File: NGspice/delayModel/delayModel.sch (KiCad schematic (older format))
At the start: 8 parts

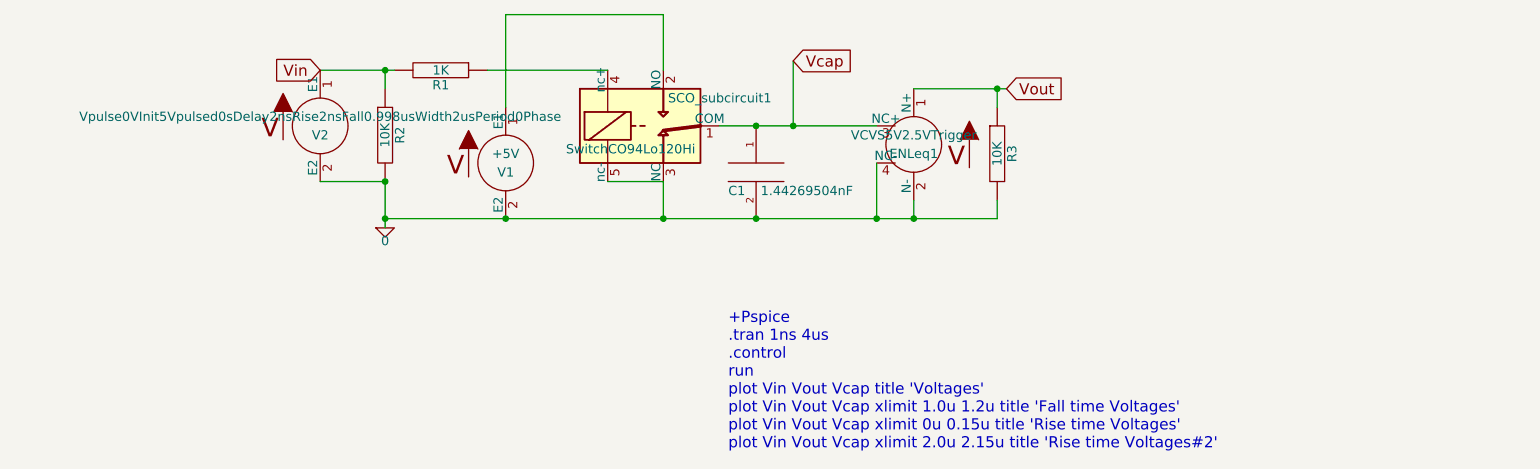
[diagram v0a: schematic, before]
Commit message: delay model completed
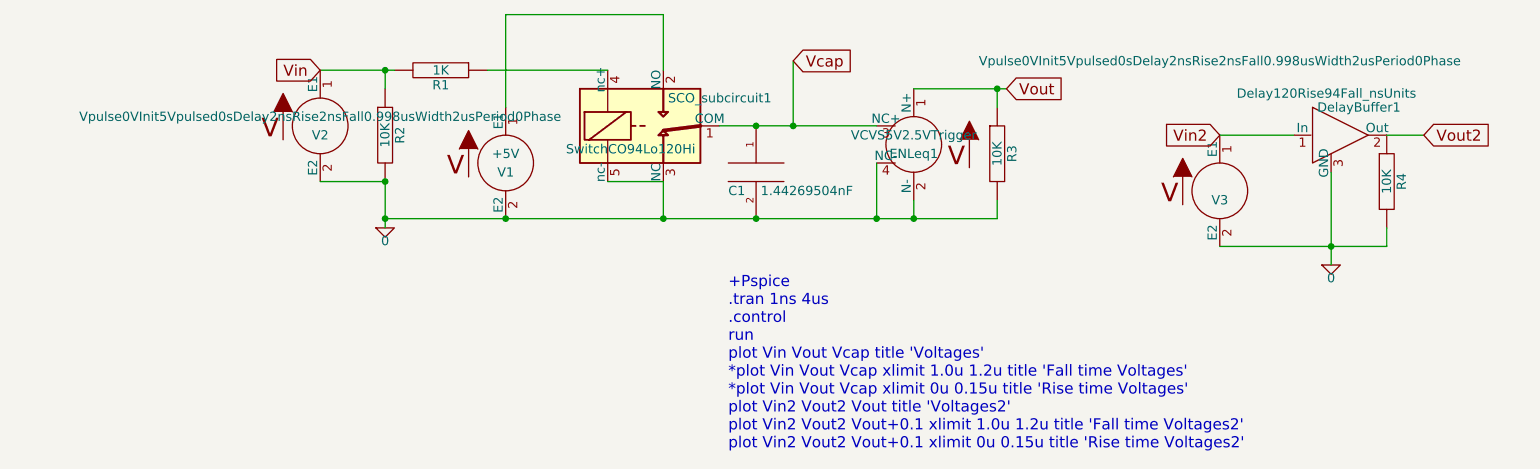
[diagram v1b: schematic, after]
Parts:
- added DelayBuffer1: Delay120Rise94Fall_nsUnits, symbol Delay120Rise94Fall_nsUnits
- added R4: 10K, symbol R
- added V3: Vpulse0VInit5Vpulsed0sDelay2nsRise2nsFall0.998usW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, symbol Vpulse0VInit5Vpulsed2nsDelay2msRise2msFall8msWidth20msPeriod0Phase
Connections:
- net 0: now also DelayBuffer1.3 (GND), R4.2, V3.2 (E2)
- new net Vin2: DelayBuffer1.1 (In), V3.1 (E1)
- new net Vout2: DelayBuffer1.2 (Out), R4.1
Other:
- note added: "+Pspice\n.tran 1ns 4us\n.control\nrun\nplot Vin Vout Vcap title 'Voltages'\n*plot Vin Vout Vcap xlimit 1.0u 1.2u title 'Fall time Voltages'\n*plot Vin Vout Vcap xlimit 0u 0.15u title 'Rise time Voltages'\nplot Vin2 Vout2 Vout title 'Voltages2'\nplot Vin2 Vout2 Vout+0.1 xlimit 1.0u 1.2u title 'Fall time Voltages2'\nplot Vin2 Vout2 Vout+0.1 xlimit 0u 0.15u title 'Rise time Voltages2'\n"
- note removed: "+Pspice\n.tran 1ns 4us\n.control\nrun\nplot Vin Vout Vcap title 'Voltages'\nplot Vin Vout Vcap xlimit 1.0u 1.2u title 'Fall time Voltages'\nplot Vin Vout Vcap xlimit 0u 0.15u title 'Rise time Voltages'\nplot Vin Vout Vcap xlimit 2.0u 2.15u title 'Rise time Voltages#2'\n"
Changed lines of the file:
@@
 	2400 1000 2400 900
 Text Notes 4250 2950 0    60   ~ 0
-+Pspice\n.tran 1ns 4us\n.control\nrun\nplot Vin Vout Vcap title 'Voltages'\nplot Vin Vout Vcap xlimit 1.0u 1.2u title 'Fall time Voltages'\nplot Vin Vout Vcap xlimit 0u 0.15u title 'Rise time Voltages'\nplot Vin Vout Vcap xlimit 2.0u 2.15u title 'Rise time Voltages#2'\n
++Pspice\n.tran 1ns 4us\n.control\nrun\nplot Vin Vout Vcap title 'Voltages'\n*plot Vin Vout Vcap xlimit 1.0u 1.2u title 'Fall time Voltages'\n*plot Vin Vout Vcap xlimit 0u 0.15u title 'Rise time Voltages'\nplot Vin2 Vout2 Vout title 'Voltages2'\nplot Vin2 Vout2 Vout+0.1 xlimit 1.0u 1.2u title 'Fall time Voltages2'\nplot Vin2 Vout2 Vout+0.1 xlimit 0u 0.15u title 'Rise time Voltages2'\n
 Connection ~ 2400 900
 Connection ~ 2400 1500
@@
 EndData
 $EndBitmap
+$Comp
+L 0 #GND02
+U 1 1 5B1863D7
+P 7500 1950
+F 0 "#GND02" H 7500 1850 50  0001 C CNN
+F 1 "0" H 7500 1880 50  0000 C CNN
+F 2 "" H 7500 1950 50  0001 C CNN
+F 3 "" H 7500 1950 50  0001 C CNN
+	1    7500 1950
+	1    0    0    -1
+$EndComp
+Wire Wire Line
+	7500 1450 7500 1950
+$Comp
+L R R4
+U 1 1 5B18642C
+P 7800 1500
+F 0 "R4" V 7880 1500 50  0000 C CNN
+F 1 "10K" V 7800 1500 50  0000 C CNN
+F 2 "" V 7730 1500 50  0001 C CNN
+F 3 "" H 7800 1500 50  0001 C CNN
+	1    7800 1500
+	1    0    0    -1
+$EndComp
+Text GLabel 8000 1250 2    60   Input ~ 0
+Vout2
+Wire Wire Line
+	8000 1250 7800 1250
+$Comp
+L Vpulse0VInit5Vpulsed2nsDelay2msRise2msFall8msWidth20msPeriod0Phase V3
+U 1 1 5B186762
+P 6900 1550
+F 0 "V3" H 6900 1500 50  0000 C CNN
+F 1 "Vpulse0VInit5Vpulsed0sDelay2nsRise2nsFall0.998usWidth2usPeriod0Phase" H 6900 2250 50  0000 C CNN
+F 2 "" H 6900 1550 50  0001 C CNN
+F 3 "" H 6900 1550 50  0001 C CNN
+	1    6900 1550
+	1    0    0    -1
+$EndComp
+Wire Wire Line
+	6900 1250 7300 1250
+Wire Wire Line
+	6900 1850 7800 1850
+Wire Wire Line
+	7800 1850 7800 1750
+Connection ~ 7500 1850
+Text GLabel 6900 1250 0    60   Input ~ 0
+Vin2
+$Comp
+L Delay120Rise94Fall_nsUnits DelayBuffer1
+U 1 1 5B186F99
+P 7550 1250
+F 0 "DelayBuffer1" H 7650 1400 50  0000 C CNN
+F 1 "Delay120Rise94Fall_nsUnits" H 7475 1475 50  0000 C CNN
+F 2 "" H 7550 1250 60  0001 C CNN
+F 3 "" H 7550 1250 60  0001 C CNN
+	1    7550 1250
+	1    0    0    -1
+$EndComp
 $EndSCHEMATC
